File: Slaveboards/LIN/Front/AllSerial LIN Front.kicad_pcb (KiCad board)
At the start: 2 copper layers, 71.5 x 24 mm, 3 parts

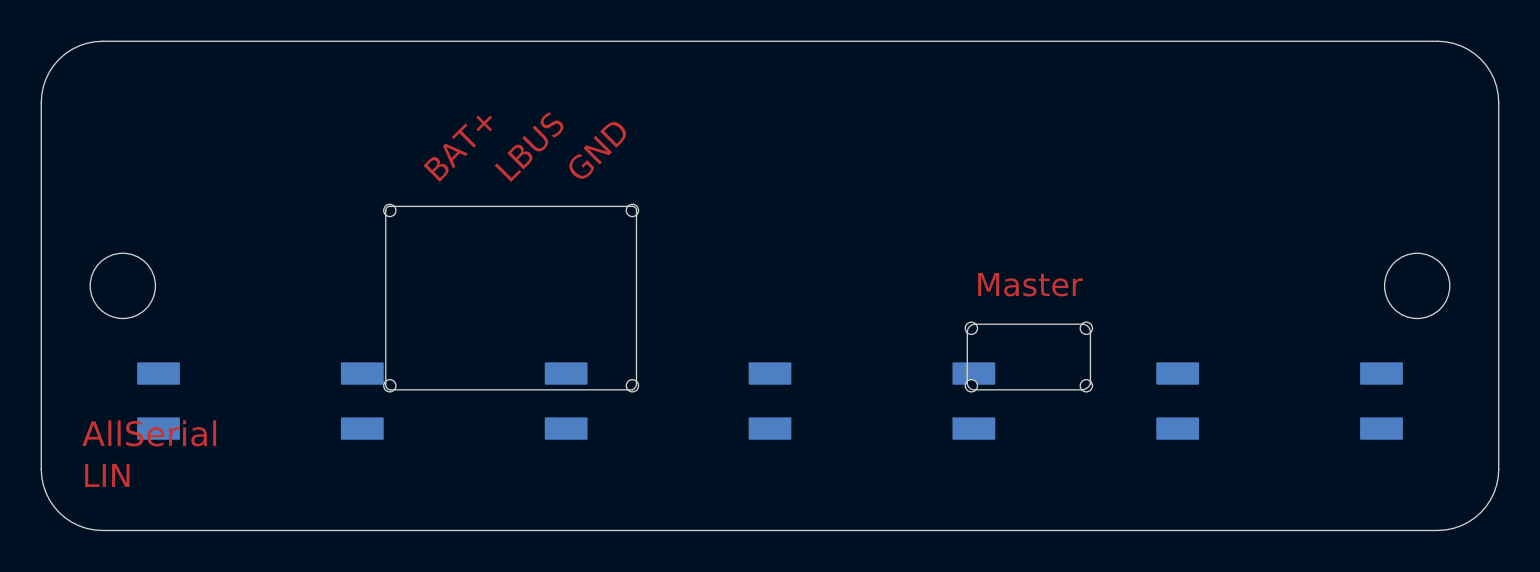
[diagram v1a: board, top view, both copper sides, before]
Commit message: improve AllSerial library
add assets for README
update README
cleanup
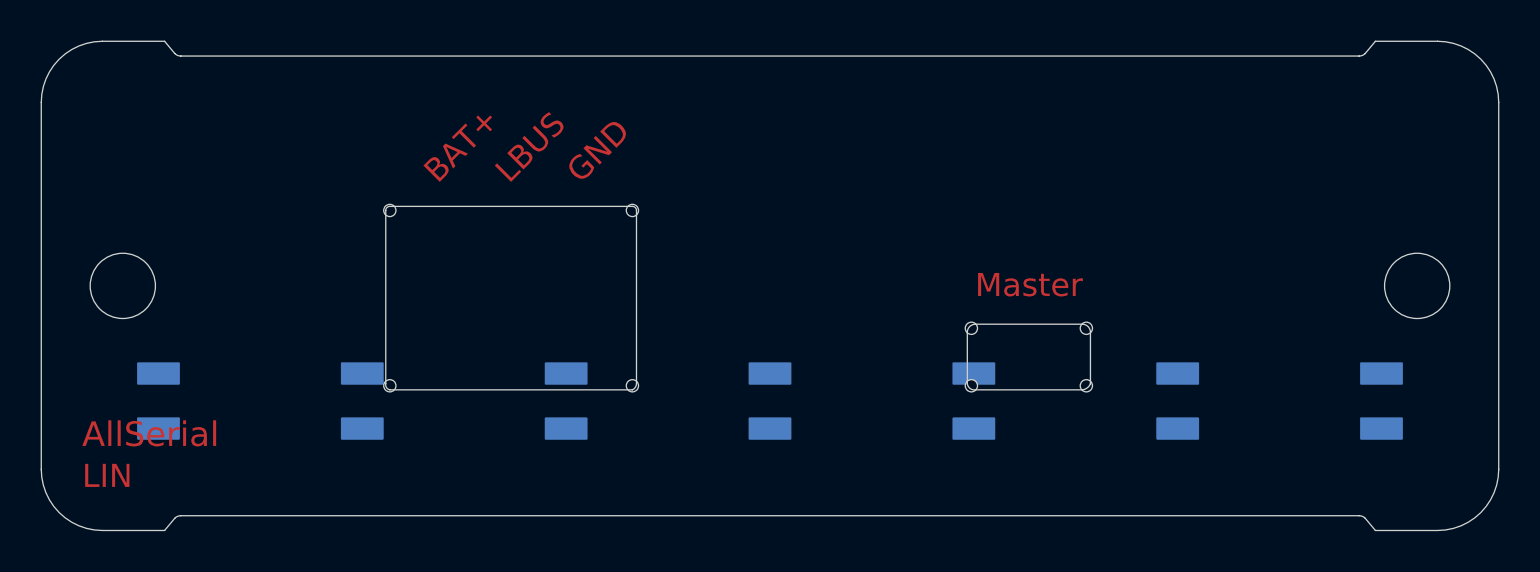
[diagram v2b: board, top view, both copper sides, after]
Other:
- outline, holes or cut-outs redrawn

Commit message: Improve libraries
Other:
- outline, holes or cut-outs redrawn
- board text added: "AllSerial LIN v1.3 27/25"
- board text added: "JLCJLCJLCJLC"
- board text removed: "AllSerial LIN v1.2 25/23"
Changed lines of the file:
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@@
-		)
-		(fp_line
-			(start -32.75 -24)
-			(end -29.7 -24)
-			(stroke
-				(width 0.05)
-				(type solid)
-			)
-			(layer "Edge.Cuts")
 		)
 		(fp_line
 			(start -32.75 0)
-			(end -29.7 0)
+			(end 32.75 0)
 			(stroke
 				(width 0.05)
@@
 		)
 		(fp_line
-			(start -29.2 -23.4)
-			(end -29.7 -24)
-			(stroke
-				(width 0.05)
-				(type default)
-			)
-			(layer "Edge.Cuts")
-		)
-		(fp_line
-			(start -29.2 -0.6)
-			(end -29.7 0)
-			(stroke
-				(width 0.05)
-				(type default)
-			)
-			(layer "Edge.Cuts")
-		)
-		(fp_line
-			(start -28.9 -23.275736)
-			(end 28.9 -23.275736)
-			(stroke
-				(width 0.05)
-				(type default)
-			)
-			(layer "Edge.Cuts")
-		)
-		(fp_line
-			(start -28.9 -0.724264)
-			(end 28.9 -0.724264)
-			(stroke
-				(width 0.05)
-				(type default)
-			)
-			(layer "Edge.Cuts")
-		)
-		(fp_line
-			(start 29.7 -24)
-			(end 29.2 -23.4)
-			(stroke
-				(width 0.05)
-				(type default)
-			)
-			(layer "Edge.Cuts")
-		)
-		(fp_line
-			(start 29.7 -24)
+			(start -32.749999 -24)
 			(end 32.75 -24)
 			(stroke
 				(width 0.05)
 				(type solid)
-			)
-			(layer "Edge.Cuts")
-		)
-		(fp_line
-			(start 29.7 0)
-			(end 29.2 -0.6)
-			(stroke
-				(width 0.05)
-				(type default)
-			)
-			(layer "Edge.Cuts")
-		)
-		(fp_line
-			(start 32.75 0)
-			(end 29.7 0)
-			(stroke
-				(width 0.05)
-				(type default)
 			)
 			(layer "Edge.Cuts")
@@
 				(width 0.05)
 				(type solid)
-			)
-			(layer "Edge.Cuts")
-		)
-		(fp_arc
-			(start -29.2 -0.6)
-			(mid -29.062359 -0.691969)
-			(end -28.9 -0.724264)
-			(stroke
-				(width 0.05)
-				(type default)
-			)
-			(layer "Edge.Cuts")
-		)
-		(fp_arc
-			(start -28.9 -23.275736)
-			(mid -29.062359 -23.308031)
-			(end -29.2 -23.4)
-			(stroke
-				(width 0.05)
-				(type default)
-			)
-			(layer "Edge.Cuts")
-		)
-		(fp_arc
-			(start 28.9 -0.724264)
-			(mid 29.062359 -0.691969)
-			(end 29.2 -0.6)
-			(stroke
-				(width 0.05)
-				(type default)
-			)
-			(layer "Edge.Cuts")
-		)
-		(fp_arc
-			(start 29.2 -23.4)
-			(mid 29.062359 -23.308031)
-			(end 28.9 -23.275736)
-			(stroke
-				(width 0.05)
-				(type default)
 			)
 			(layer "Edge.Cuts")
@@
 		)
 	)
-	(gr_text "AllSerial LIN v1.2 25/23"
+	(gr_text "AllSerial LIN v1.3 27/25"
 		(at 148.5011 97.5036 0)
 		(layer "B.SilkS")
@@
 		)
 	)
+	(gr_text "JLCJLCJLCJLC"
+		(at 156.2011 114.5036 0)
+		(layer "B.SilkS")
+		(effects
+			(font
+				(size 1 1)
+				(thickness 0.1)
+			)
+			(justify left bottom mirror)
+		)
+	)

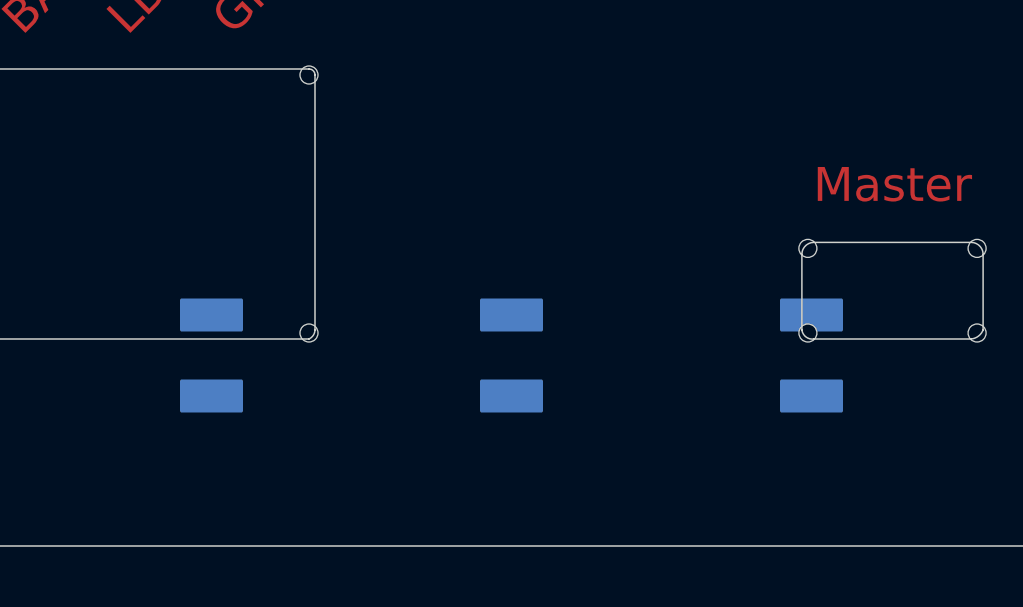
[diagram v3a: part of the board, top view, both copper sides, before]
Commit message: Remove pads from cutouts
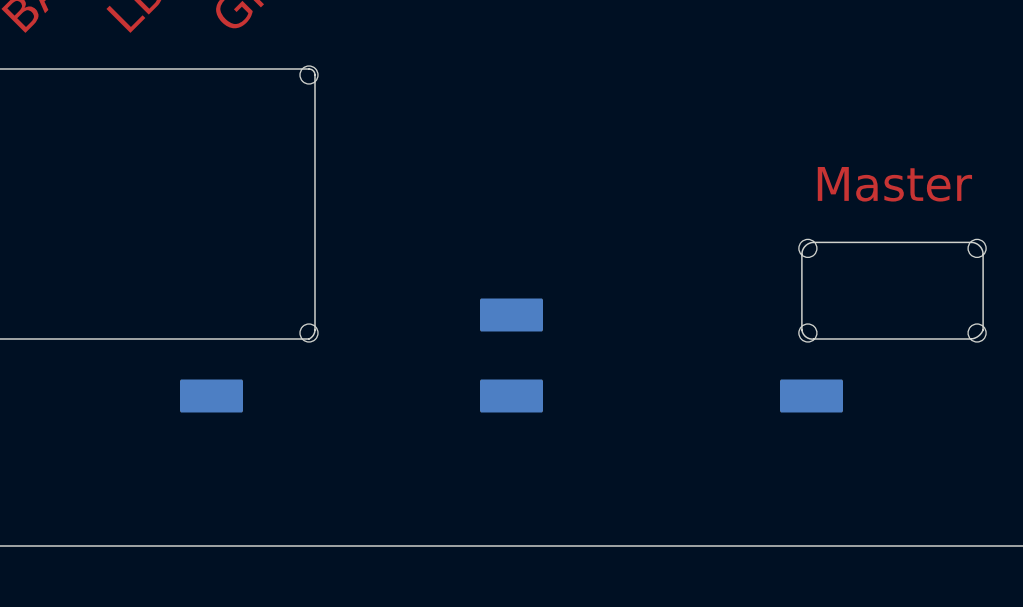
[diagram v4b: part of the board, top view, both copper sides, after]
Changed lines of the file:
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@@
-		)
-		(fp_rect
-			(start -11 -8.2)
-			(end -9 -7.2)
-			(stroke
-				(width 0.1)
-				(type solid)
-			)
-			(fill yes)
-			(layer "B.Cu")
 		)
 		(fp_rect
@@
 			(start -1 -5.5)
 			(end 1 -4.5)
-			(stroke
-				(width 0.1)
-				(type solid)
-			)
-			(fill yes)
-			(layer "B.Cu")
-		)
-		(fp_rect
-			(start 9 -8.2)
-			(end 11 -7.2)
 			(stroke
 				(width 0.1)
@@
 		)
 		(fp_rect
-			(start -11 -8.2)
+			(start -11 -5.55)
 			(end -9 -4.5)
 			(stroke
@@
 		)
 		(fp_rect
-			(start 9 -8.2)
+			(start 9 -5.5)
 			(end 11 -4.5)
 			(stroke

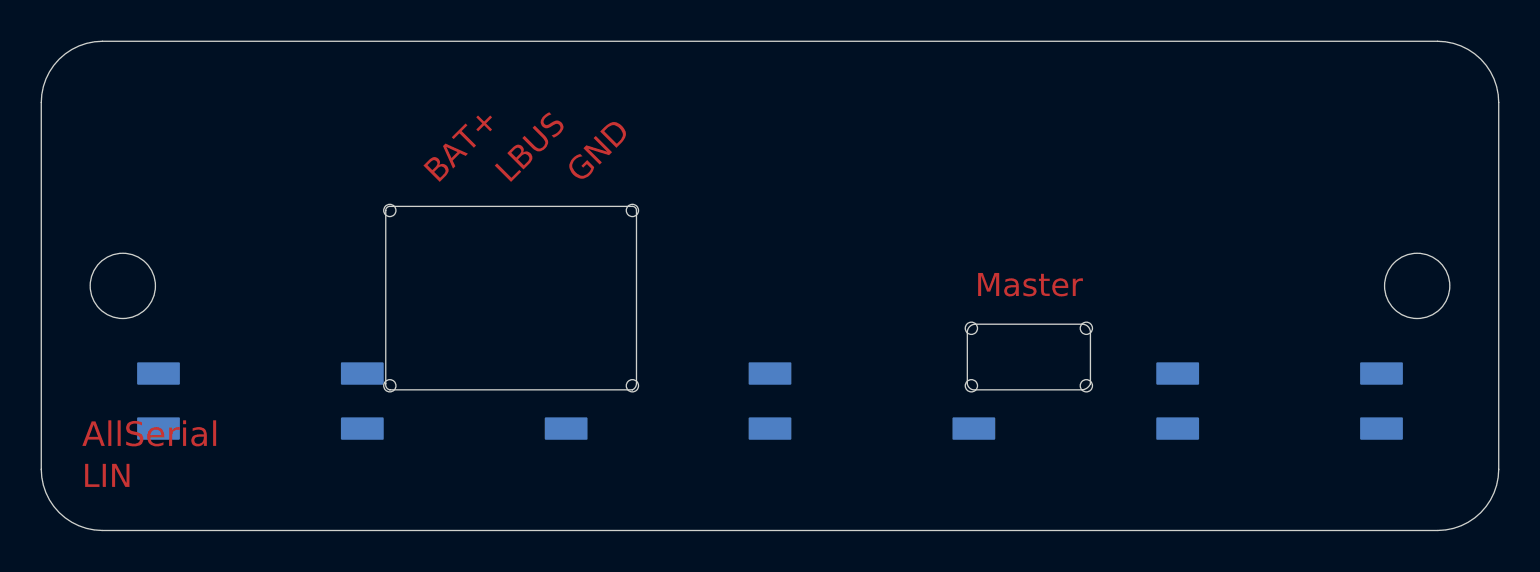
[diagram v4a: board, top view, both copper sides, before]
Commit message: Add python testskript
Add mainboard tester
Add libraries
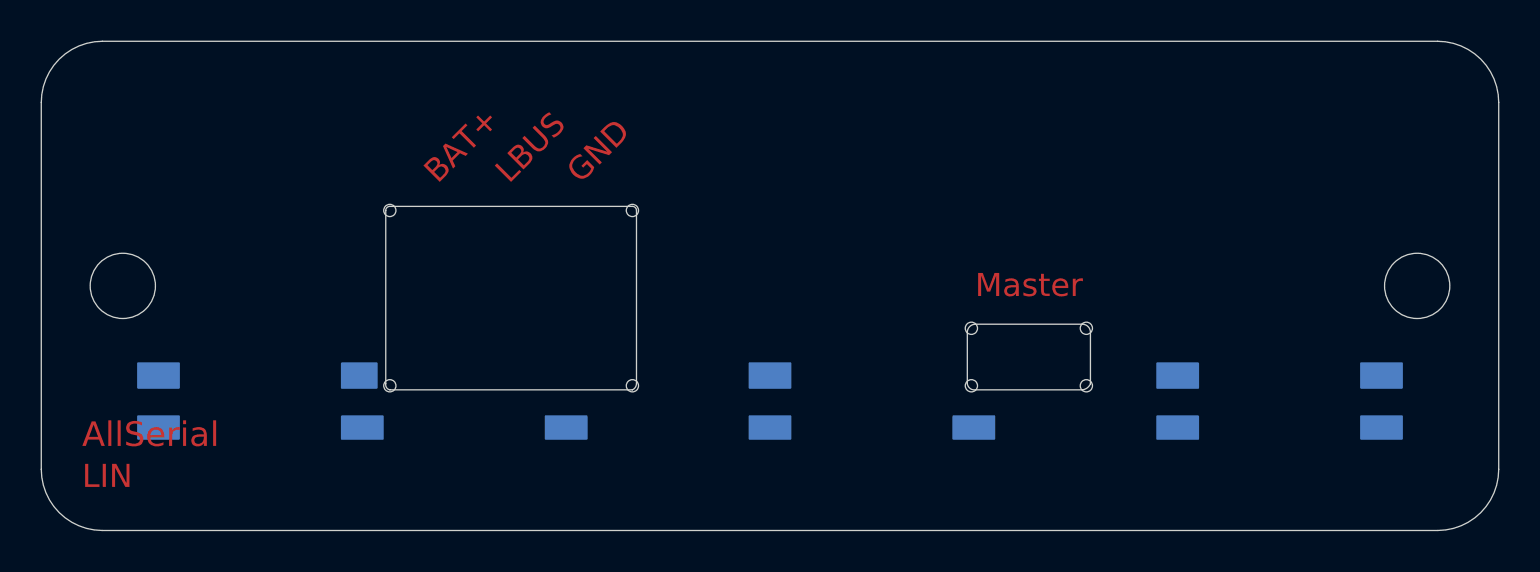
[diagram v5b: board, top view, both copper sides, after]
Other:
- board text removed: "JLCJLCJLCJLC"
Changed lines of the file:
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@@
 		(fp_rect
 			(start -31 -8.2)
-			(end -29 -7.2)
+			(end -29 -7)
 			(stroke
 				(width 0.1)
@@
 		)
 		(fp_rect
-			(start -31 -5.5)
+			(start -31 -5.6)
 			(end -29 -4.5)
 			(stroke
@@
 		(fp_rect
 			(start -21 -8.2)
-			(end -19 -7.2)
+			(end -19.3 -7)
 			(stroke
 				(width 0.1)
@@
 		)
 		(fp_rect
-			(start -21 -5.5)
+			(start -21 -5.6)
 			(end -19 -4.5)
 			(stroke
@@
 		)
 		(fp_rect
-			(start -11 -5.5)
+			(start -11 -5.6)
 			(end -9 -4.5)
 			(stroke
@@
 		(fp_rect
 			(start -1 -8.2)
-			(end 1 -7.2)
+			(end 1 -7)
 			(stroke
 				(width 0.1)
@@
 		)
 		(fp_rect
-			(start -1 -5.5)
+			(start -1 -5.6)
 			(end 1 -4.5)
 			(stroke
@@
 		)
 		(fp_rect
-			(start 9 -5.5)
+			(start 9 -5.6)
 			(end 11 -4.5)
 			(stroke
@@
 		(fp_rect
 			(start 19 -8.2)
-			(end 21 -7.2)
+			(end 21 -7)
 			(stroke
 				(width 0.1)
@@
 		)
 		(fp_rect
-			(start 19 -5.5)
+			(start 19 -5.6)
 			(end 21 -4.5)
 			(stroke
@@
 		(fp_rect
 			(start 29 -8.2)
-			(end 31 -7.2)
+			(end 31 -7)
 			(stroke
 				(width 0.1)
@@
 		)
 		(fp_rect
-			(start 29 -5.5)
+			(start 29 -5.6)
 			(end 31 -4.5)
 			(stroke
@@
 		)
 		(fp_rect
-			(start -11 -5.55)
+			(start -11 -8.2)
 			(end -9 -4.5)
 			(stroke
@@
 		)
 		(fp_rect
-			(start 9 -5.5)
+			(start 9 -8.2)
 			(end 11 -4.5)
 			(stroke
@@
 	)
 	(gr_text "AllSerial LIN v1.3 27/25"
-		(at 148.5011 97.5036 0)
+		(at 148.5011 98.3346 0)
 		(layer "B.SilkS")
 		(effects
@@
 		)
 	)
-	(gr_text "JLCJLCJLCJLC"
-		(at 156.2011 114.5036 0)
-		(layer "B.SilkS")
-		(effects
-			(font
-				(size 1 1)
-				(thickness 0.1)
-			)
-			(justify left bottom mirror)
-		)
-	)
